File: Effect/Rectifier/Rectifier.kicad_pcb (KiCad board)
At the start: 2 copper layers, 32 x 75 mm, 36 parts, among them J1 Conn_01x03_Pin, J2 Conn_01x03_Pin, U1 OPA1656, U2 OPA1656

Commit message: Update all the PCB's with the recent changes from simulation
Time to get another set of test boards manufactured, this time perhaps
with the high-frequency oscillation fixed for good thanks to much
improved simulations.

And maybe the tremolo works with blinking LEDs too.  I added another
one, because I'm using the same enclosure for all of these, so I need to
put *something* in the holes that are drilled...

Signed-off-by: Linus Torvalds <torvalds@linux-foundation.org>
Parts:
- C10: value 10pF -> 47pF
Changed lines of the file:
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@@
 			)
 		)
-		(property "Value" "10pF"
+		(property "Value" "47pF"
 			(at 0 1.68 90)
 			(layer "F.Fab")
@@
 			)
 		)
-		(property "Sim.Params" "r=100k"
+		(property "Sim.Params" "r=100k pos=0.2"
 			(at 0 0 90)
 			(unlocked yes)
@@
 			)
 		)
-		(property "Sim.Params" "r=100k"
+		(property "Sim.Params" "r=100k pos=0.7"
 			(at 0 0 90)
 			(unlocked yes)
@@
 			)
 		)
-		(property "Sim.Params" "r=10k pos=1.0"
+		(property "Sim.Params" "r=10k pos=0.5"
 			(at 0 0 90)
 			(unlocked yes)

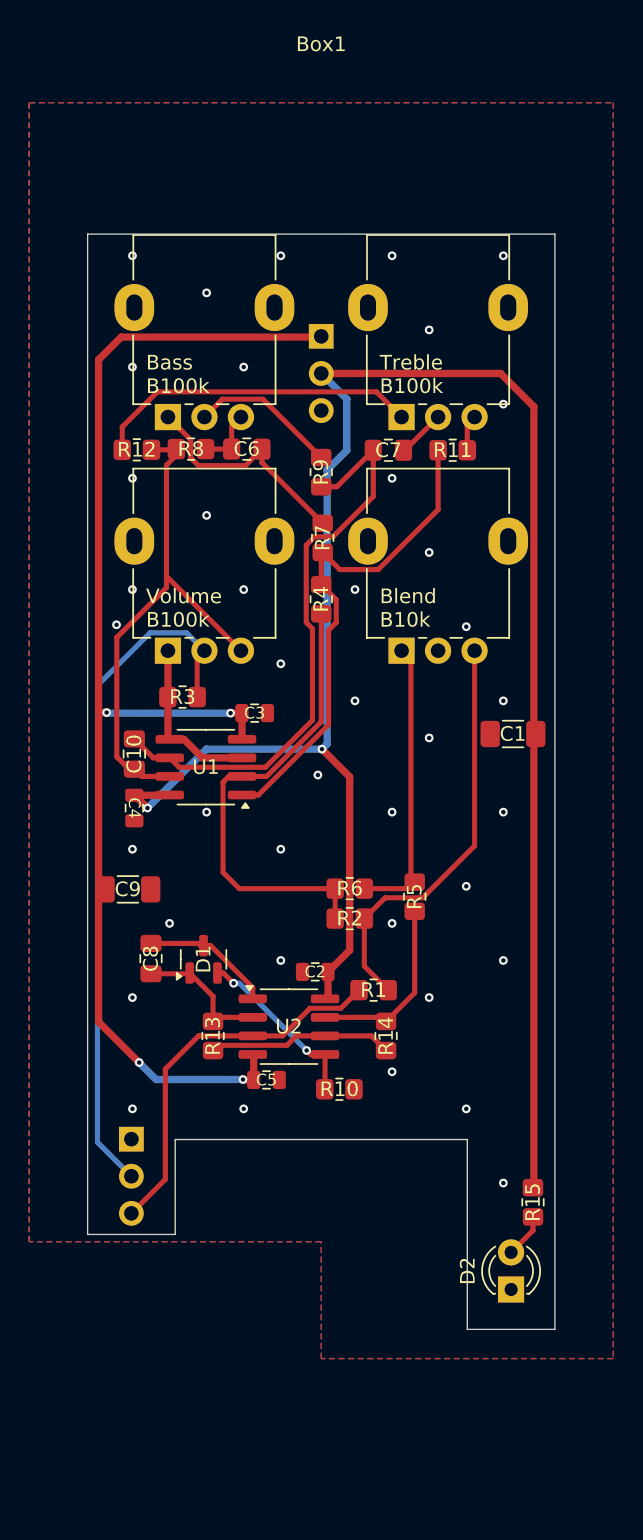
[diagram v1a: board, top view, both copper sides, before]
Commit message: Convert rectifier board to KiCad 9
.. and do the shield pin and connect the potentiometer bodies up to it.

Same problems with the netlist as with the boost board, of course.

Signed-off-by: Linus Torvalds <torvalds@linux-foundation.org>
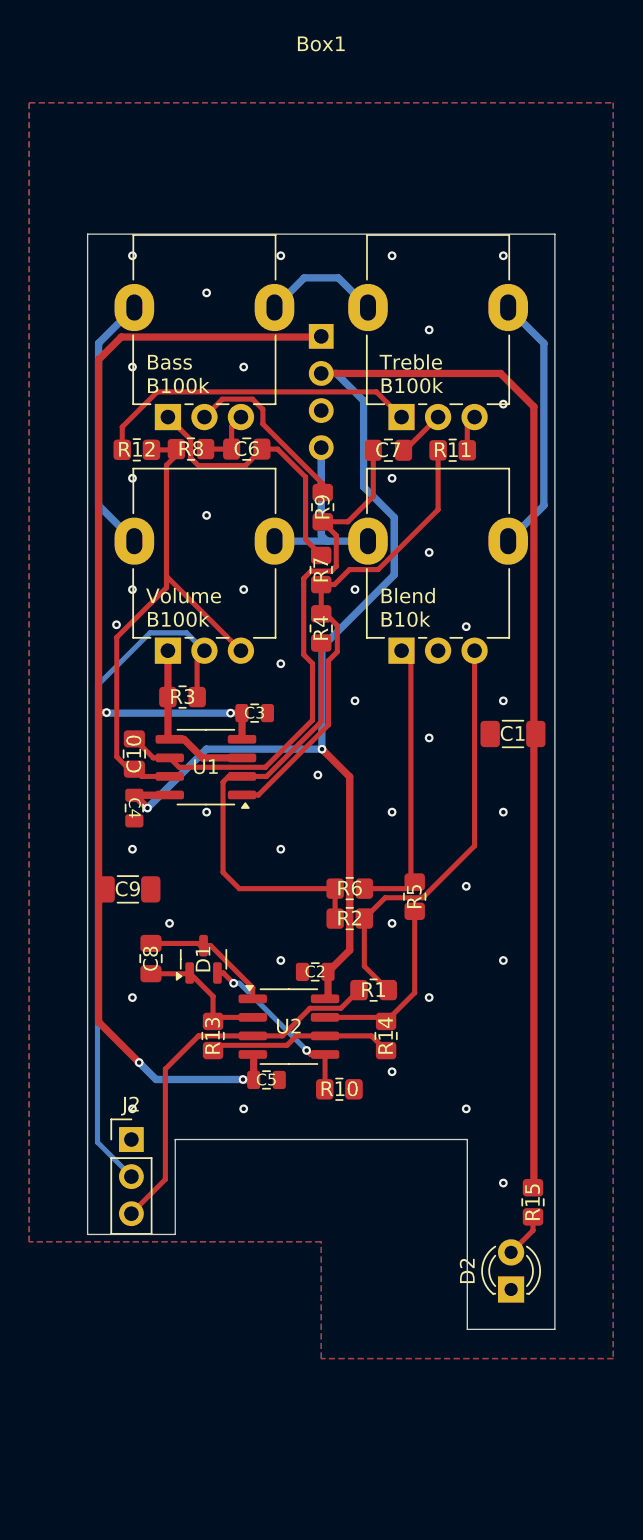
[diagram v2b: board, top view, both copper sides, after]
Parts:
- J1: value Conn_01x03_Pin -> Conn_01x04_Pin; footprint Connector_PinHeader_2.54mm:PinHeader_1x03_P2.54mm_Vertical -> Connector_PinHeader_2.54mm:PinHeader_1x04_P2.54mm_Vertical
- J2: moved to F.Cu
- moved R9 2.40 mm to (100.1, 81.7)
- moved R7 2.20 mm to (100.0, 86.0)
- moved R4 2.00 mm to (100.0, 90.0)
- turned J2 to 0 degrees
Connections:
- RV1 pad : (no net) -> SHIELD
- RV2 pad : (no net) -> SHIELD
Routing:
- net (no net): track 0.00 -> 44.1 mm
- net SHIELD: track 0.00 -> 13.0 mm
- net +V: track 131.9 -> 135.2 mm
- net Net-(C6-Pad1): track 15.8 -> 18.6 mm
- net Net-(U1B--): track 40.2 -> 37.6 mm
- net Net-(R9-Pad1): track 10.2 -> 12.2 mm
- net Net-(U1A--): track 32.2 -> 30.2 mm
- net OUT^{BLEND}: track 34.0 -> 32.2 mm

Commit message: Version N+1 of the rectifier board
I have enjoyed the design side of the precision rectifier circuit.  The
concept of the circuit - rater than the resulting distortion - was
admittedly why I started it in the first place.

The idea was that the rectifier could be used for other things than as
the actual signal output (ie using it as the peak detector in a
compression pedal or whatever).  But using it as the distortion itself
was kind of the first step.

But I have to admit to really not liking the *sound* of the resulting
octaver fuzz.  I think it's too much fizz, and the alleged octave-up
side is entirely drowned in all the high-order harmonics.

So I have a cunning plan: replace the Baxandall tone control with a
rather aggressive second-order low-pass filter.  That should counter-
act the harsh signal spikes when the polarity of the signal changes, and
for some frequencies will (at least in simulation with a pure sine-wave)
result in a pretty clean octave-up effect.

Will this be a better sound? Who knows.  But it's certainly a different
one.  And the Baxandall tone circuit was already done - and worked
fairly well - in the regular diode-clipping overdrive pedal.

This also tunes the diode choice for the rectification a bit, simply
because I started looking at different diodes in simulation.  A
low-V_{f} Schottky diode simulates better in that critical polarity
change region, but who knows how accurate the spice models here are.

Anyway, for the common cheap SOT-23-3 diodes in series (so that I can
just try different footprints) the BAT54S simulated best out of the ones
I tried.  The Rohm RB706WM-40 simulated even better, but doesn't exist
in SOT-23-3.

Put another way: this is another step in the "Linus learns about random
analog circuits".  This time the new circuit being a low-pass Sallen-Key
filter to hopefully make the octaver fuzz pedal sound better.  Or at
least sound different.

Signed-off-by: Linus Torvalds <torvalds@linux-foundation.org>
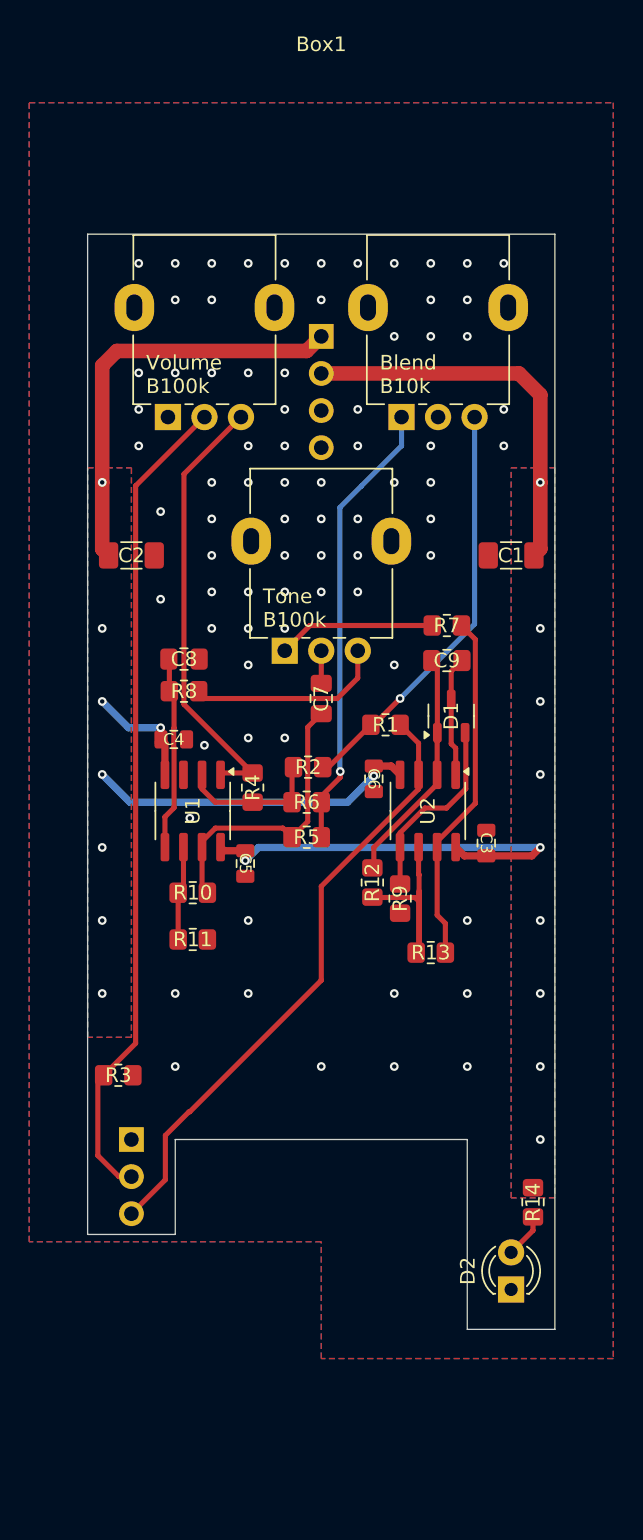
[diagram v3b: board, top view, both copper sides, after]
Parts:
- removed C10: 47pF, Capacitor_SMD:C_0805_2012Metric_Pad1.18x1.45mm_HandSolder
- removed the C6 at (94.9, 77.7)
- removed the R12 at (87.4, 77.8)
- removed the R9 at (100.1, 81.7)
- removed RV4: Treble B100k, Potentiometer_THT:Potentiometer_Alpha_RD901F-40-00D_Single_Vertical
- added C8: 4.7nF, Capacitor_SMD:C_0805_2012Metric_Pad1.18x1.45mm_HandSolder, F.Cu at (90.6, 92.1)
- added R10: 10k, Resistor_SMD:R_0805_2012Metric_Pad1.20x1.40mm_HandSolder, F.Cu at (91.2, 108.1)
- C7: value 560pF -> 4.7nF
- D1: value MMBD1203 -> BAT54S; footprint Package_TO_SOT_SMD:SOT-23 -> Package_TO_SOT_SMD:SOT-23-3
- J2: moved to B.Cu
- R12: renamed from R13; value 1k -> 10k
- R13: renamed from R14; value 1k -> 10k
- R5, R6: value 10k -> 15k
- R7, R8: value 22k -> 4.7k
- R9: renamed from R10; value 1k -> 10k
- RV3: value Bass B100k -> Tone B100k
- moved R11 37.9 mm to (91.2, 111.3), turned to 0 degrees
- moved C9 28.8 mm to (108.6, 92.2), turned to 0 degrees
- moved R3 26.3 mm to (86.1, 120.6), turned to 0 degrees
- moved D1 23.8 mm to (108.9, 96.0)
- moved C2 22.9 mm to (87.0, 85.0)
- moved C6 21.9 mm to (103.6, 100.3), turned to -90 degrees
- moved R1 18.2 mm to (104.4, 96.6), turned to 0 degrees
- moved RV3 17.9 mm to (97.5, 91.5)
- moved C7 17.6 mm to (100.0, 94.8), turned to -90 degrees
- moved U2 17.6 mm to (107.3, 102.5), turned to -90 degrees
- moved R8 16.6 mm to (90.6, 94.3), turned to 180 degrees
- moved RV1 16.0 mm to (105.5, 75.5)
- moved RV2 16.0 mm to (89.5, 75.5)
- moved R12 15.1 mm to (103.5, 107.4)
- moved C3 14.7 mm to (111.3, 104.7), turned to 90 degrees
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- renumbered C9 to C2, C2 to C3, C3 to C4, C4 to C5, C5 to C6, C8 to C9, R15 to R14, RV2 to RV1, RV1 to RV2
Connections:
- C7 pad 1: Net-(U1B--) -> Net-(C7-Pad1)
- C7 pad 2: Net-(C7-Pad2) -> FILTERED
- R11 pad 1: Net-(R11-Pad1) -> Net-(U1B--)
- R11 pad 2: OUT^{BLEND} -> GND
- R5 pad 2: RECT -> FILTERED
- R7 pad 1: Net-(C6-Pad1) -> RECT
- R7 pad 2: OUT^{BLEND} -> Net-(R7-Pad2)
- R8 pad 1: OUT^{BAX} -> Net-(R8-Pad1)
- R8 pad 2: Net-(C6-Pad2) -> Net-(U1B-+)
- RV1 pad : SHIELD -> (no net)
- RV2 pad : SHIELD -> (no net)
- RV2 pad 3: OUT^{BAX} -> OUT^{BLEND}
- RV3 pad 1: Net-(C6-Pad1) -> Net-(R7-Pad2)
- RV3 pad 2: Net-(R9-Pad1) -> Net-(C7-Pad1)
- RV3 pad 3: Net-(C6-Pad2) -> Net-(R8-Pad1)
- U1 pad 5: GND -> Net-(U1B-+)
- U1 pad 7: OUT^{BAX} -> FILTERED
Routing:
- net +V: track 135.2 -> 56.1 mm, vias 2 -> 10
- net (no net): track 44.1 -> 0.00 mm
- net OUT^{BAX}: track 35.4 -> 0.00 mm
- net Net-(U1B--): track 37.6 -> 6.48 mm
- net -V: track 86.9 -> 60.4 mm, vias 4 -> 9
- net Net-(R12-Pad2): track 22.4 -> 0.00 mm
- net Net-(U1A--): track 30.2 -> 9.95 mm
- net FILTERED: track 0.00 -> 19.8 mm
- net Net-(C6-Pad1): track 18.6 -> 0.00 mm
- net IN: track 26.3 -> 42.2 mm
- net Net-(R8-Pad1): track 0.00 -> 13.6 mm
- net Net-(U1B-+): track 0.00 -> 13.3 mm
- net SHIELD: track 13.0 -> 0.00 mm
- net Net-(R9-Pad1): track 12.2 -> 0.00 mm
- net RECT: track 12.3 -> 24.1 mm
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- added copper zone on B.Cu, net +V
- added copper zone on F.Cu, net +V
- added copper zone on B.Cu, net -V
- added copper zone on F.Cu, net -V
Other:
- board text added: "Tone B100k"
- board text removed: "Bass B100k"
- board text removed: "Treble B100k"

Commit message: Clean up and finish re-org of the the octaver pedal too
The octaver pedal is trying to no longer be so much of a fuzz, and
trying much harder to be a cleaner octave-up pedal instead.  And I've
simulated it more to try to make it so, and that we don't have any
nassty oscillation issues.

Whether those simulations pan out with better sounds, we will have to
just wait and see..

Signed-off-by: Linus Torvalds <torvalds@linux-foundation.org>
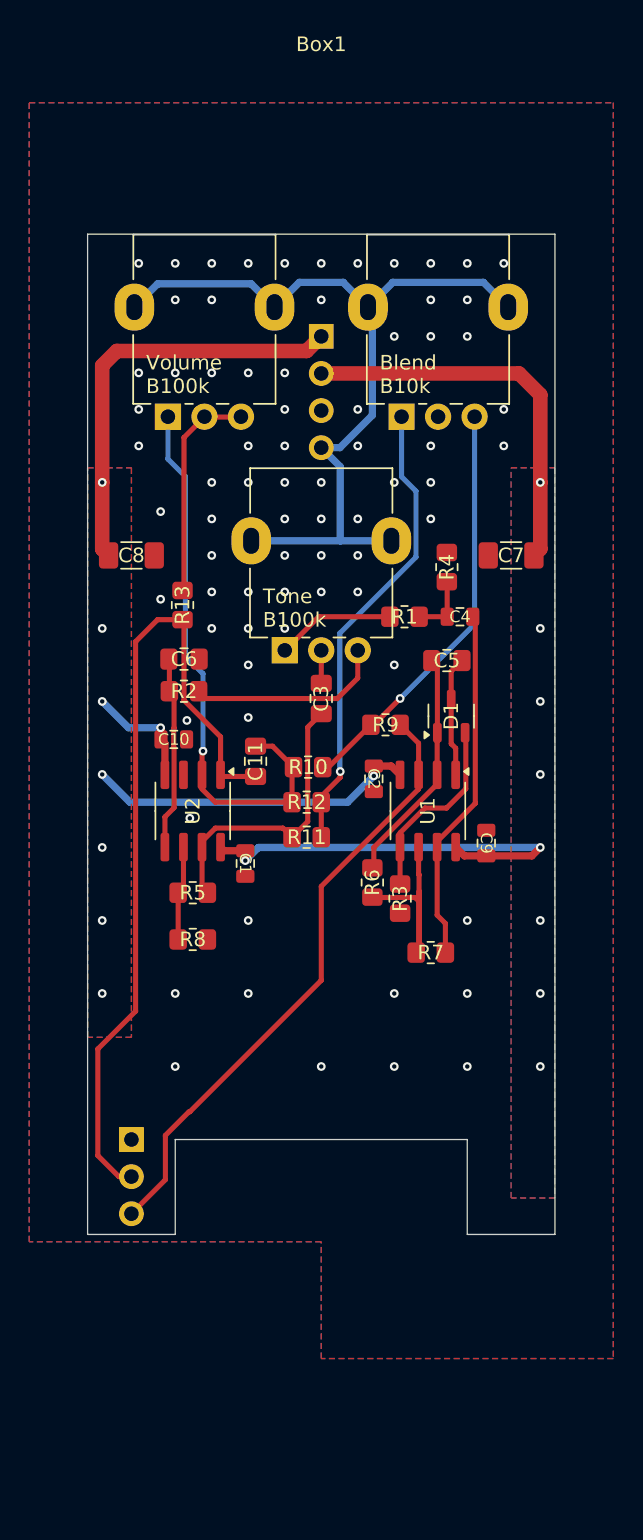
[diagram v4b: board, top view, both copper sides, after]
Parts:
- removed D2: LED, LED_THT:LED_D3.0mm
- removed R14: 10k, Resistor_SMD:R_0805_2012Metric_Pad1.20x1.40mm_HandSolder
- removed the R3 at (86.1, 120.6)
- added C11: 47pF, Capacitor_SMD:C_0805_2012Metric_Pad1.18x1.45mm_HandSolder, F.Cu at (95.5, 99.1)
- added C4: 0.1uF, Mylib:C_0704_1810Metric, F.Cu at (109.5, 89.2)
- added R13: 15k, Resistor_SMD:R_0805_2012Metric_Pad1.20x1.40mm_HandSolder, F.Cu at (90.5, 88.4)
- R11: renamed from R5; value 15k -> 10k
- R12: renamed from R6; value 15k -> 10k
- R4: value 51k -> 470k
- RV1: value Blend B10k -> B100k Tone; footprint Potentiometer_THT:Potentiometer_Alpha_RD901F-40-00D_Single_Vertical -> Mylib:Potentiometer_9mm_MP
- RV2: value Volume B100k -> B10k Blend; footprint Potentiometer_THT:Potentiometer_Alpha_RD901F-40-00D_Single_Vertical -> Mylib:Potentiometer_9mm_MP
- RV3: value Tone B100k -> B100k Volume; footprint Potentiometer_THT:Potentiometer_Alpha_RD901F-40-00D_Single_Vertical -> Mylib:Potentiometer_9mm_MP
- moved RV3 24.2 mm to (92.0, 68.0), turned to 0 degrees
- moved R4 20.1 mm to (108.6, 85.8)
- moved RV2 20.0 mm to (108.0, 68.0), turned to 0 degrees
- moved RV1 10.1 mm to (100.0, 84.0), turned to 0 degrees
- moved R1 2.96 mm to (105.7, 89.2)
- renumbered C5 to C1, C4 to C10, C6 to C2, C7 to C3, C9 to C5, C8 to C6, C1 to C7, C2 to C8, C3 to C9, R7 to R1, R2 to R10, R8 to R2, R9 to R3, R10 to R5, R12 to R6, R13 to R7, R11 to R8, R1 to R9, U2 to U1, U1 to U2
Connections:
- C3 pad 1: Net-(C7-Pad1) -> Net-(C3-Pad1)
- R1 pad 1: RECT -> Net-(C4-Pad1)
- R1 pad 2: Net-(R7-Pad2) -> Net-(R1-Pad2)
- R10 pad 1: Net-(U1A--) -> Net-(U2A--)
- R10 pad 2: Net-(R1-Pad1) -> Net-(R10-Pad2)
- R11 pad 1: Net-(R5-Pad1) -> Net-(R11-Pad1)
- R12 pad 1: Net-(U1A--) -> Net-(U2A--)
- R12 pad 2: Net-(R5-Pad1) -> Net-(R11-Pad1)
- R2 pad 1: Net-(R8-Pad1) -> Net-(R2-Pad1)
- R4 pad 1: OUT^{BLEND} -> GND
- R4 pad 2: Net-(U1A--) -> Net-(C4-Pad1)
- R9 pad 1: Net-(R1-Pad1) -> Net-(R10-Pad2)
- RV1 pad 1: Net-(R5-Pad1) -> Net-(R1-Pad2)
- RV1 pad 2: GND -> Net-(C3-Pad1)
- RV1 pad 3: Net-(R1-Pad1) -> Net-(R2-Pad1)
- RV2 pad 1: GND -> Net-(R11-Pad1)
- RV2 pad 2: OUT -> GND
- RV2 pad 3: OUT^{BLEND} -> Net-(R10-Pad2)
- RV3 pad 1: Net-(R7-Pad2) -> Net-(U2A--)
- RV3 pad 2: Net-(C7-Pad1) -> Net-(R13-Pad2)
- RV3 pad 3: Net-(R8-Pad1) -> Net-(R13-Pad2)
- U2 pad 1: OUT^{BLEND} -> OUT
- U2 pad 2: Net-(U1A--) -> Net-(U2A--)
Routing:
- net SHIELD: track 0.00 -> 60.1 mm
- net Net-(U2A--): track 0.00 -> 38.5 mm, vias 0 -> 1
- net Net-(R11-Pad1): track 0.00 -> 31.5 mm, vias 0 -> 1
- net Net-(R5-Pad1): track 31.1 -> 0.00 mm, vias 1 -> 0
- net OUT^{BLEND}: track 30.2 -> 0.00 mm
- net Net-(R1-Pad1): track 28.6 -> 0.00 mm, vias 1 -> 0
- net Net-(R10-Pad2): track 0.00 -> 28.0 mm, vias 0 -> 1
- net Net-(R13-Pad2): track 0.00 -> 15.0 mm
- net Net-(R8-Pad1): track 13.6 -> 0.00 mm
- net Net-(R2-Pad1): track 0.00 -> 13.6 mm
- net Net-(R7-Pad2): track 10.8 -> 0.00 mm
- net Net-(U1A--): track 9.95 -> 0.00 mm
- net Net-(R1-Pad2): track 0.00 -> 8.16 mm
- net Net-(C4-Pad1): track 0.00 -> 4.34 mm
- net Net-(D2-A): track 3.05 -> 0.00 mm
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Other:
- board size 32 x 75 mm -> 32 x 68.5 mm

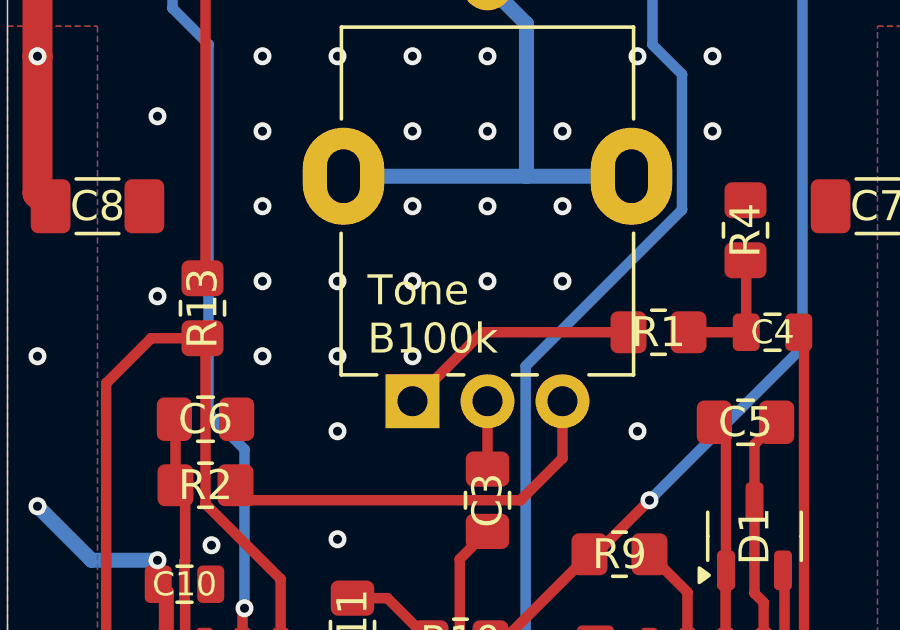
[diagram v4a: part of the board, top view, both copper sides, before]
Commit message: Update some of the rectifier values and commentary
This board actually sounds fun, and I have positive feedback from an
actual real guitar player.  But the "Tone" knob is mislabeled, and the
range of it should be adjusted.

It's more properly called "Weird", and instead of the normal flat Q=1
being in the middle, that boring normal setting should be at the
beginning of the pot, and it should go weird from there.

In the old model, going the other way (turning the tone knob down from
the middle) really didn't do anything interesting, so half of the range
of the knob was pretty useless.

But other than that kind of fairly minor details, it's been a success in
this form.

I think the range of the Weird pot could/should probably still be played
with, and in particular I suspect it might be worth looking into adding
resistors between the wiper and the ends to allow modifying the taper of
the pot to make the interesting range more useful.

But that's for a future date.

Signed-off-by: Linus Torvalds <torvalds@linux-foundation.org>
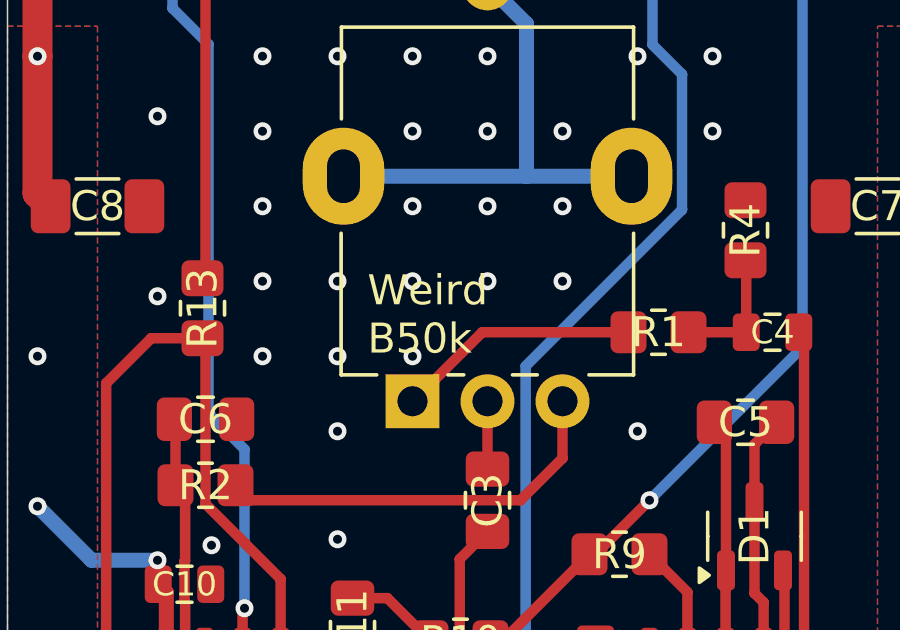
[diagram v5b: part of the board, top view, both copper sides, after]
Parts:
- R1: value 4.7k -> 56k
- RV1: value B100k Tone -> B50k Weird
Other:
- board text added: "Weird B50k"
- board text removed: "Tone B100k"
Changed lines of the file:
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@@
 			)
 		)
-		(property "Value" "B100k Tone"
+		(property "Value" "B50k  Weird"
 			(at 0 -6.5 0)
 			(unlocked yes)
@@
 			)
 		)
-		(property "Sim.Params" "r=100k"
+		(property "Sim.Params" "r=100k pos=1"
 			(at 0 0 0)
 			(unlocked yes)
@@
 			)
 		)
-		(property "Value" "4.7k"
+		(property "Value" "56k"
 			(at 0 1.65 0)
 			(layer "F.Fab")
@@
 			)
 		)
-		(property "Sim.Params" "r=10k pos=0"
+		(property "Sim.Params" "r=10k pos=1"
 			(at 0 0 0)
 			(unlocked yes)
@@
 		)
 	)
-	(gr_text "Tone\nB100k"
+	(gr_text "Weird\nB50k"
 		(at 96 90 0)
 		(layer "F.SilkS")
